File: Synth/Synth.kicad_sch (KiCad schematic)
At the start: 0 parts

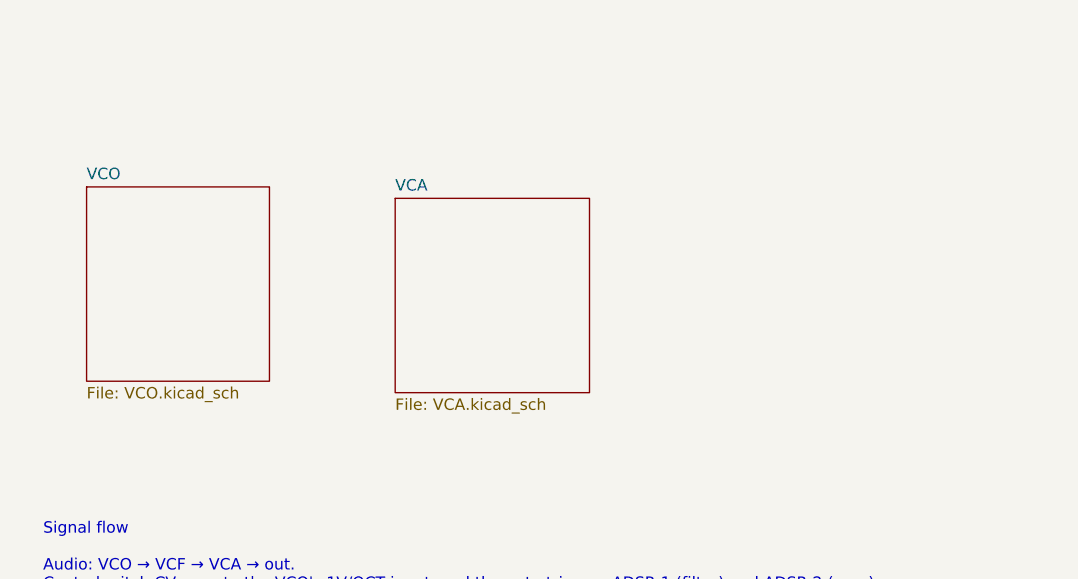
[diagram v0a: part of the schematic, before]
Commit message: added components
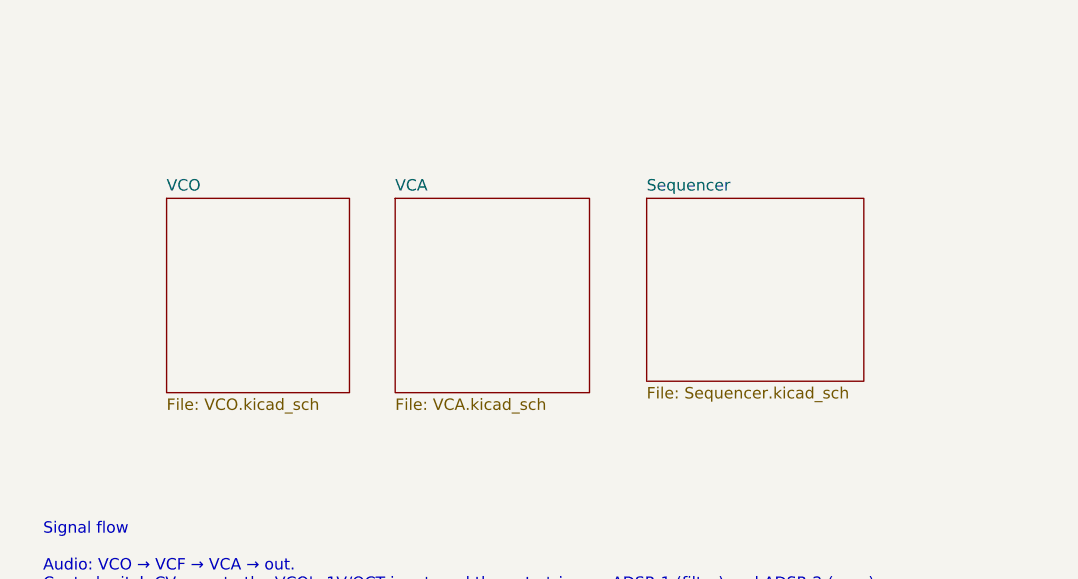
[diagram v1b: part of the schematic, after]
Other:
- added sheet Sequencer (Sequencer.kicad_sch)
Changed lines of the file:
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@@
+	)
+	(sheet
+		(at 88.9 33.02)
+		(size 24.13 20.32)
+		(fields_autoplaced yes)
+		(stroke
+			(width 0.1524)
+			(type solid)
+		)
+		(fill
+			(color 0 0 0 0.0000)
+		)
+		(property "Sheetname" "Sequencer"
+			(at 88.9 32.3084 0)
+			(effects
+				(font
+					(size 1.27 1.27)
+				)
+				(justify left bottom)
+			)
+		)
+		(property "Sheetfile" "Sequencer.kicad_sch"
+			(at 88.9 53.9246 0)
+			(effects
+				(font
+					(size 1.27 1.27)
+				)
+				(justify left top)
+			)
+		)
+		(property "Field2" ""
+			(at 88.9 33.02 0)
+			(effects
+				(font
+					(size 1.27 1.27)
+				)
+				(hide yes)
+			)
+		)
+		(instances
+			(project "Synth"
+				(path "/ec39c741-f5f8-424a-a9fe-47b13645d3cb"
+					(page "4")
+				)
+			)
+		)
 	)
 	(sheet
@@
 	)
 	(sheet
-		(at 26.67 31.75)
+		(at 35.56 33.02)
 		(size 20.32 21.59)
 		(fields_autoplaced yes)
@@
 		)
 		(property "Sheetname" "VCO"
-			(at 26.67 31.0384 0)
+			(at 35.56 32.3084 0)
 			(effects
 				(font
@@
 		)
 		(property "Sheetfile" "VCO.kicad_sch"
-			(at 26.67 53.9246 0)
+			(at 35.56 55.1946 0)
 			(effects
 				(font
@@
 		)
 		(property "Field2" ""
-			(at 26.67 31.75 0)
+			(at 35.56 33.02 0)
 			(effects
 				(font
